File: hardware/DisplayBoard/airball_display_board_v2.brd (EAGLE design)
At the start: 69 x 107 mm, 46 parts, among them J2 105450-0101, J4 105450-0101, J5 SCREW_TERMINAL_8POS, J6 SCREW_TERMINAL_8POS, SW1 TL1014BF160QG, SW2 TL1014BF160QG, SW3 TL1014BF160QG, SW4 TL1014BF160QG, SW5 TL1014BF160QG, U10 DS3231, U2 TFP401A, U3 TFT_40PIN_FFC-BOT, U5 TPS61169

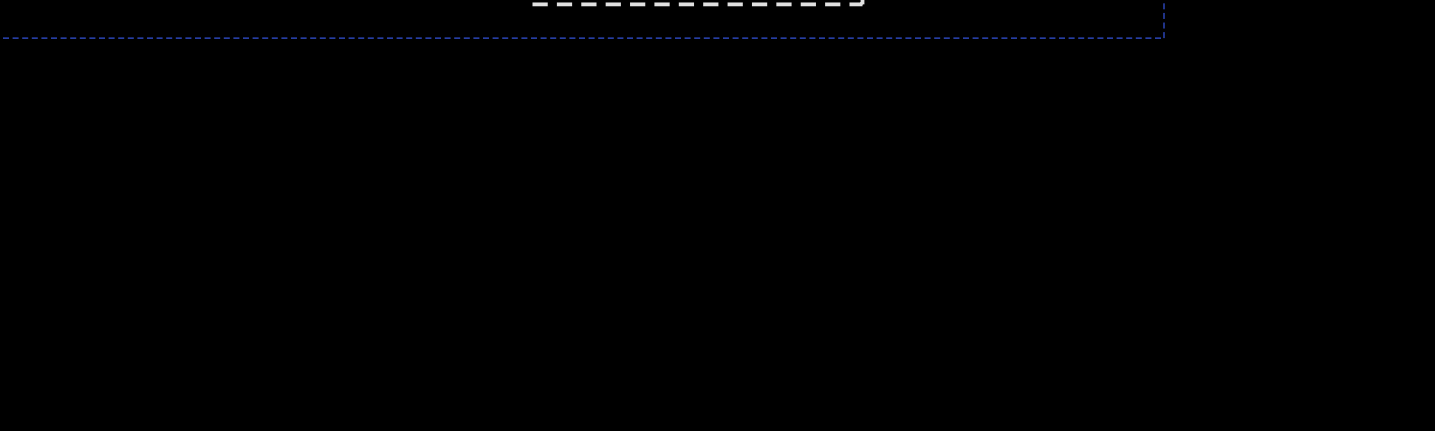
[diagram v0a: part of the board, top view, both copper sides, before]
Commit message: Cleaned up schematic
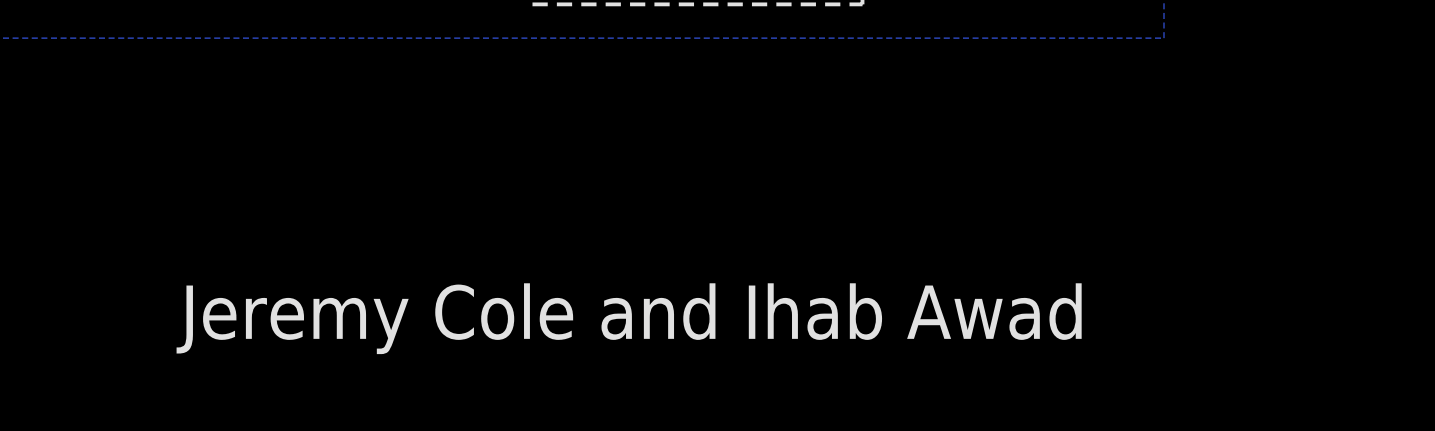
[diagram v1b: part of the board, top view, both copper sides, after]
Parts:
- added FRAME1, FRAME2, FRAME3, FRAME4, FRAME5: FRAME-LETTER, SparkFun-Aesthetics:CREATIVE_COMMONS
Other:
- board text added: "Jeremy Cole and Ihab Awad"
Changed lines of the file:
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@@
 <text x="61.5" y="27.5" size="1.778" layer="21" font="fixed" rot="R90" align="top-center">http://airball.aero/</text>
 <text x="42.2" y="20.3" size="0.8128" layer="21" font="vector">D1</text>
+<text x="40.4" y="-14.4" size="1.778" layer="21">Jeremy Cole and Ihab Awad</text>
 </plain>
 <attributes>
@@
 <attribute name="VALUE" x="37.012" y="18.25" size="0.6096" layer="27" font="vector" ratio="20" rot="R90" align="top-center"/>
 </element>
+<element name="FRAME4" library="SparkFun-Aesthetics" package="CREATIVE_COMMONS" value="FRAME-LETTER" x="13.3" y="-14.2" smashed="yes">
+<attribute name="DESIGNER" value="" x="13.3" y="-14.2" size="1.778" layer="27" display="off"/>
+<attribute name="REV" value="" x="13.3" y="-14.2" size="1.778" layer="27" display="off"/>
+</element>
+<element name="FRAME1" library="SparkFun-Aesthetics" package="CREATIVE_COMMONS" value="FRAME-LETTER" x="13.3" y="-22.9" smashed="yes">
+<attribute name="DESIGNER" value="" x="13.3" y="-22.9" size="1.778" layer="27" display="off"/>
+<attribute name="REV" value="" x="13.3" y="-22.9" size="1.778" layer="27" display="off"/>
+</element>
+<element name="FRAME2" library="SparkFun-Aesthetics" package="CREATIVE_COMMONS" value="FRAME-LETTER" x="13.3" y="-31.6" smashed="yes">
+<attribute name="DESIGNER" value="" x="13.3" y="-31.6" size="1.778" layer="27" display="off"/>
+<attribute name="REV" value="" x="13.3" y="-31.6" size="1.778" layer="27" display="off"/>
+</element>
+<element name="FRAME3" library="SparkFun-Aesthetics" package="CREATIVE_COMMONS" value="FRAME-LETTER" x="13.3" y="-40.3" smashed="yes">
+<attribute name="DESIGNER" value="" x="13.3" y="-40.3" size="1.778" layer="27" display="off"/>
+<attribute name="REV" value="" x="13.3" y="-40.3" size="1.778" layer="27" display="off"/>
+</element>
+<element name="FRAME5" library="SparkFun-Aesthetics" package="CREATIVE_COMMONS" value="FRAME-LETTER" x="13.3" y="-49" smashed="yes">
+<attribute name="DESIGNER" value="" x="13.3" y="-49" size="1.778" layer="27" display="off"/>
+<attribute name="REV" value="" x="13.3" y="-49" size="1.778" layer="27" display="off"/>
+</element>
 </elements>

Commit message: Minor improvements to display board.
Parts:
- removed J2, J4: 105450-0101, 105450-0101:MOLEX_105450-0101
- added 34, J7: DX07S016JA1R1500, airball:JAE_DX07S016JA1R1500
- moved R3 8.14 mm to (10.3, 52.7), turned to 180 degrees
- moved R4 6.25 mm to (10.3, 54.5), turned to 180 degrees
- moved R1 1.75 mm to (33.6, 10.1)
- moved R2 1.75 mm to (35.2, 10.1)
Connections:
- net GND: now also 34.1, 34.12, 34.S1, 34.S2, 34.S3, 34.S4, 34.S5, 34.S6, J7.1, J7.12, J7.S1, J7.S2, J7.S3, J7.S4, J7.S5, J7.S6; no longer J2.A1, J2.A12, J2.B1, J2.B12, J2.S1, J2.S2, J2.S3, J2.S4, J4.A1, J4.A12, J4.B1, J4.B12, J4.S1, J4.S2, J4.S3, J4.S4
- net N$1: now also 34.9; no longer J2.B5
- net N$2: now also 34.3; no longer J2.A5
- net N$3: now also J7.9; no longer J4.B5
- net N$4: now also J7.3; no longer J4.A5
- net VCC_5V0: now also 34.11, 34.2, J7.11, J7.2; no longer J2.A4, J2.A9, J2.B4, J2.B9, J4.A4, J4.A9, J4.B4, J4.B9
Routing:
- net VCC_5V0: track 203.1 -> 190.0 mm, vias 10 -> 6
- net N$3: track 9.88 -> 3.54 mm
- net GND: track 5.37 -> 0.00 mm
- net N$4: track 7.14 -> 3.76 mm
- net USB_P: track 58.0 -> 60.6 mm
- net USB_N: track 59.1 -> 60.9 mm, vias 2 -> 0
- net N$2: track 2.35 -> 3.45 mm
- net N$1: track 4.43 -> 3.33 mm
